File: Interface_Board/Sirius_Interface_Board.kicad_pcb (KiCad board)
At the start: 2 copper layers, 157 x 65 mm, 20 parts, among them J1 KB1, J10 TO_VIDEO, J11 JOYSTICK, J12 TO_JOYSTICK, J13 TO_RESET, J15 DIN5, J2 TO_KB1, J3 KB2, J4 TO_KB2, J5 POWER, J6 TO_POWER, J7 TAPE, J8 TO_TAPE, J9 AUDIO, SW1 RESET

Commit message: Finalised test PCB design
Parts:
- moved H6 1.76 mm to (230.3, 88.2)
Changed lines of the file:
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@@
 		(allow_soldermask_bridges_in_footprints no)
 		(tenting front back)
-		(grid_origin 153.924402 55.686809)
+		(grid_origin 266.3298 105.1573)
 		(pcbplotparams
 			(layerselection 0x00000000_00000000_55555555_5755f5ff)
@@
 	(footprint "MountingHole:MountingHole_3.2mm_M3"
 		(layer "F.Cu")
-		(at 232 87.6)
+		(at 230.3298 88.1573)
 		(descr "Mounting Hole 3.2mm, no annular, M3")
 		(tags "mounting hole 3.2mm no annular m3")
@@
 					(size 1.016 0.9144)
 					(thickness 0.2032)
-					(italic yes)
 				)
 			)
@@
 	)
 	(gr_text "RESET"
-		(locked yes)
 		(at 209.0254 59.9169 0)
 		(layer "F.SilkS")
@@
 	)
 	(segment
-		(start 225.77 100.405)
-		(end 230.965 105.6)
+		(start 225.6098 84.6998)
+		(end 225.6098 100.2448)
 		(width 0.2)
 		(layer "F.Cu")
@@
 	)
 	(segment
-		(start 225.77 84.86)
-		(end 225.77 100.405)
+		(start 225.6098 100.2448)
+		(end 230.965 105.6)
 		(width 0.2)
 		(layer "F.Cu")
@@
 	(segment
 		(start 223.64 82.73)
-		(end 225.77 84.86)
+		(end 225.6098 84.6998)
 		(width 0.2)
 		(layer "F.Cu")
@@
 	)
 	(segment
-		(start 226.78 83.33)
-		(end 226.78 98.875)
+		(start 223.64 80.19)
+		(end 226.3698 82.9198)
 		(width 0.2)
 		(layer "F.Cu")
@@
 	)
 	(segment
-		(start 226.78 98.875)
-		(end 233.505 105.6)
+		(start 226.3698 82.9198)
+		(end 226.3698 98.4648)
 		(width 0.2)
 		(layer "F.Cu")
@@
 	)
 	(segment
-		(start 223.64 80.19)
-		(end 226.78 83.33)
+		(start 226.3698 98.4648)
+		(end 233.505 105.6)
 		(width 0.2)
 		(layer "F.Cu")
@@
 	)
 	(segment
-		(start 227.750131 97.305131)
+		(start 227.1798 96.7348)
 		(end 236.045 105.6)
 		(width 0.2)
@@
 	)
 	(segment
-		(start 227.750131 81.760131)
-		(end 227.750131 97.305131)
+		(start 223.64 77.65)
+		(end 227.1798 81.1898)
 		(width 0.2)
 		(layer "F.Cu")
@@
 	)
 	(segment
-		(start 223.64 77.65)
-		(end 227.750131 81.760131)
+		(start 227.1798 81.1898)
+		(end 227.1798 96.7348)
 		(width 0.2)
 		(layer "F.Cu")
@@
 	)
 	(group ""
-		(locked yes)
-		(members "284b52d0-4ed5-4a7a-885b-3ee70c460cc6" "2879ccf7-4c23-40b6-ba66-4d1f54aaeb5e"
-			"578e50c0-ebb7-4968-a88f-0dda1ec3fe24" "998cf33d-528e-40b0-ab5f-cc9450b6f5d9"
-			"e5696d8b-0ffd-4da7-9f46-33fc6edbfca2" "eaeea273-3af0-4986-8c87-85b5155f2b2b"
-			"f244ef54-7bb8-4fe2-b5d1-fa7e1b6c0899" "f3a2c414-2732-4044-9f24-c8c751f2aac6"
-		)
-	)
-	(group ""

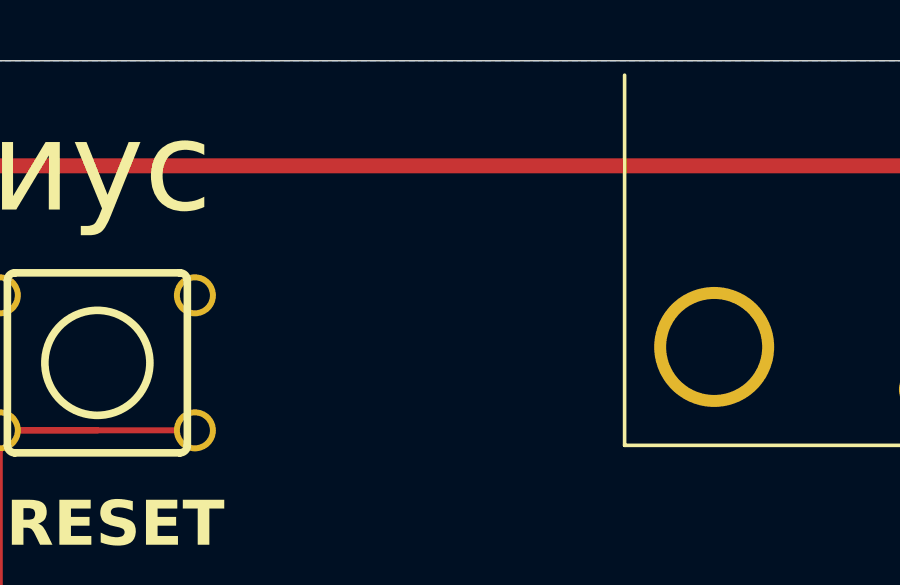
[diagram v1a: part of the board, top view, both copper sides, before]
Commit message: Added some text to PCB
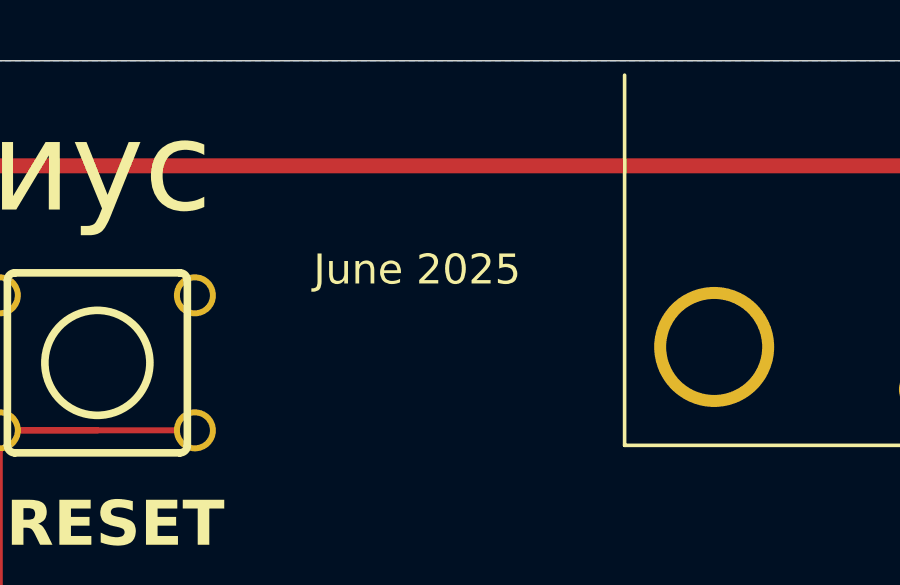
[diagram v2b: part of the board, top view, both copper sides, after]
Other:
- board text added: "Interface board for СИРИУС Brett Hallen, June 2025 www.youtube.com/@Brfff"
- board text added: "June 2025"
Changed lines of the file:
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@@
+		)
+	)
+	(gr_text "June 2025"
+		(at 219.2698 51.1473 0)
+		(layer "F.SilkS")
+		(effects
+			(font
+				(size 1 1)
+				(thickness 0.1)
+			)
+			(justify left bottom)
+		)
+	)
+	(gr_text "Interface board for СИРИУС\nBrett Hallen, June 2025\nwww.youtube.com/@Brfff"
+		(at 266.1398 75.4273 0)
+		(layer "B.SilkS")
+		(effects
+			(font
+				(size 1 1)
+				(thickness 0.1)
+			)
+			(justify left bottom mirror)
 		)
 	)
